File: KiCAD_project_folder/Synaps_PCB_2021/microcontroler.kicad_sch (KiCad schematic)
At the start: 35 parts, among them IC2 ESP32-S2, SW3 SW_Push, SW4 SW_Push, U3 AT25DF041x-UxN-x, Y2 40 MHz, Y3 32.768 KHz

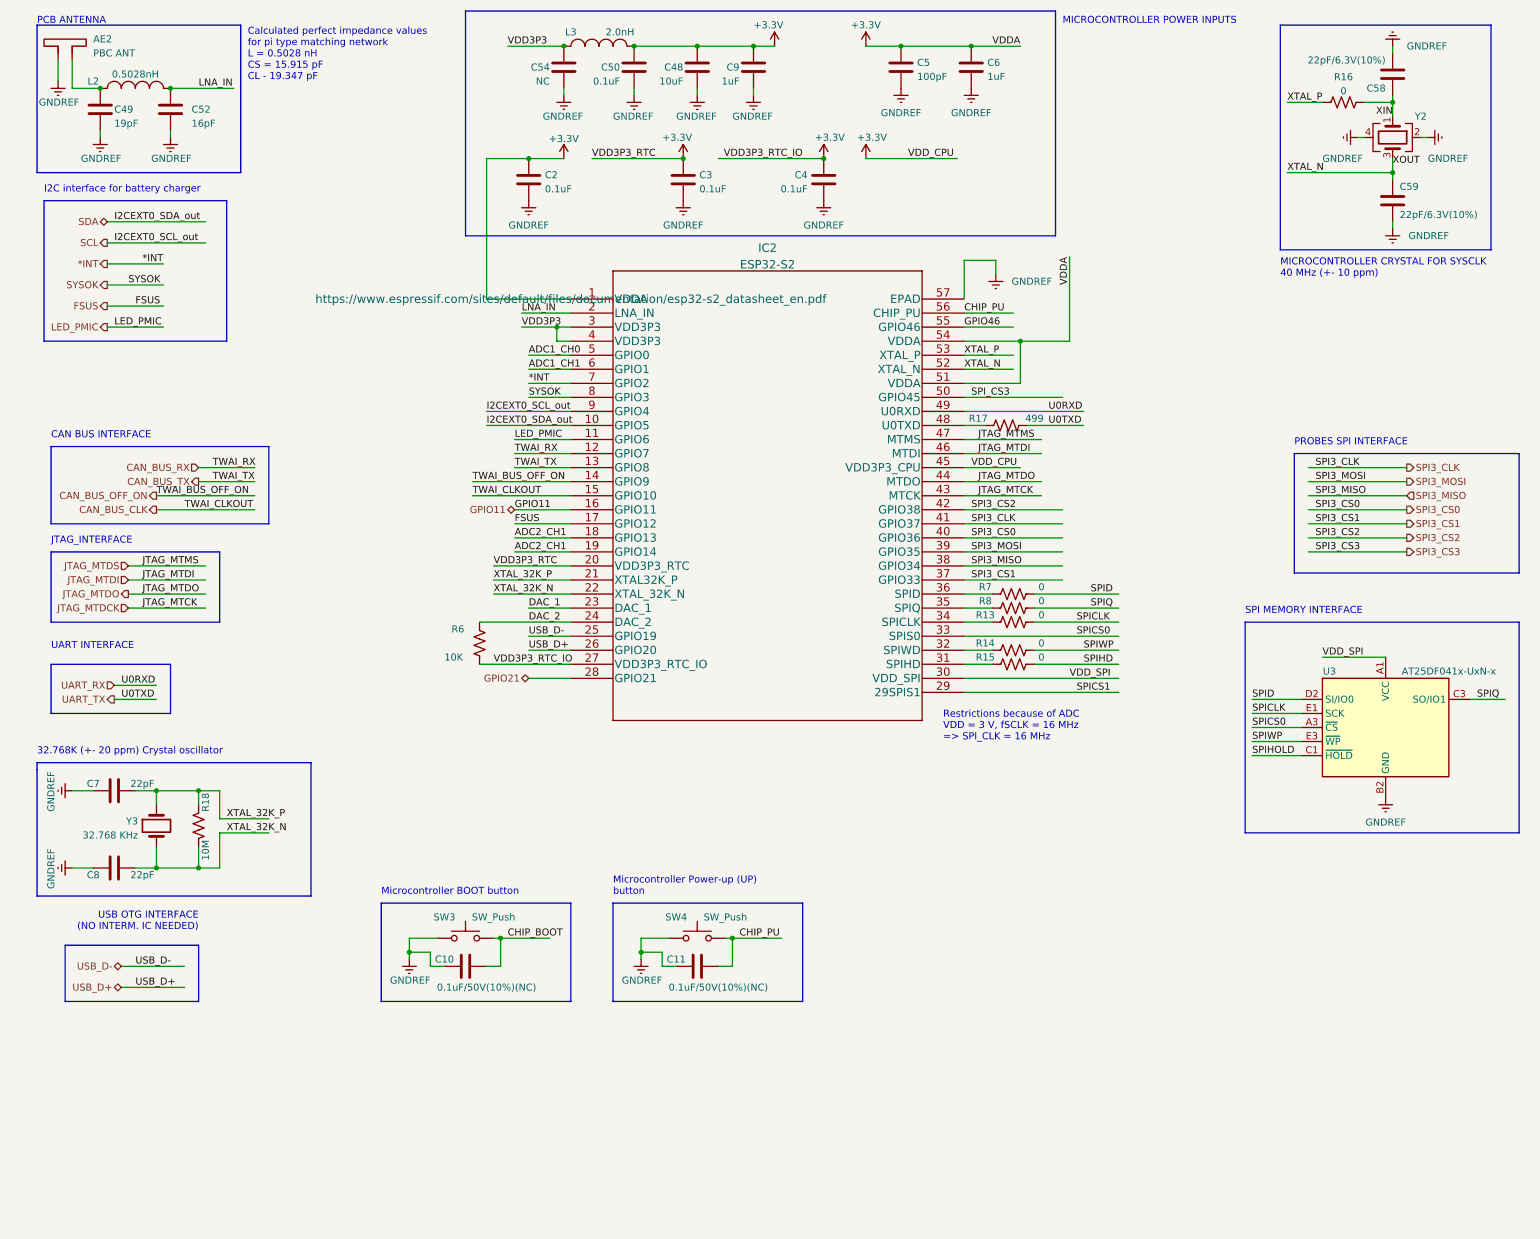
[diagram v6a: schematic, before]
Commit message: Transistionned board to ESP32S3, wip
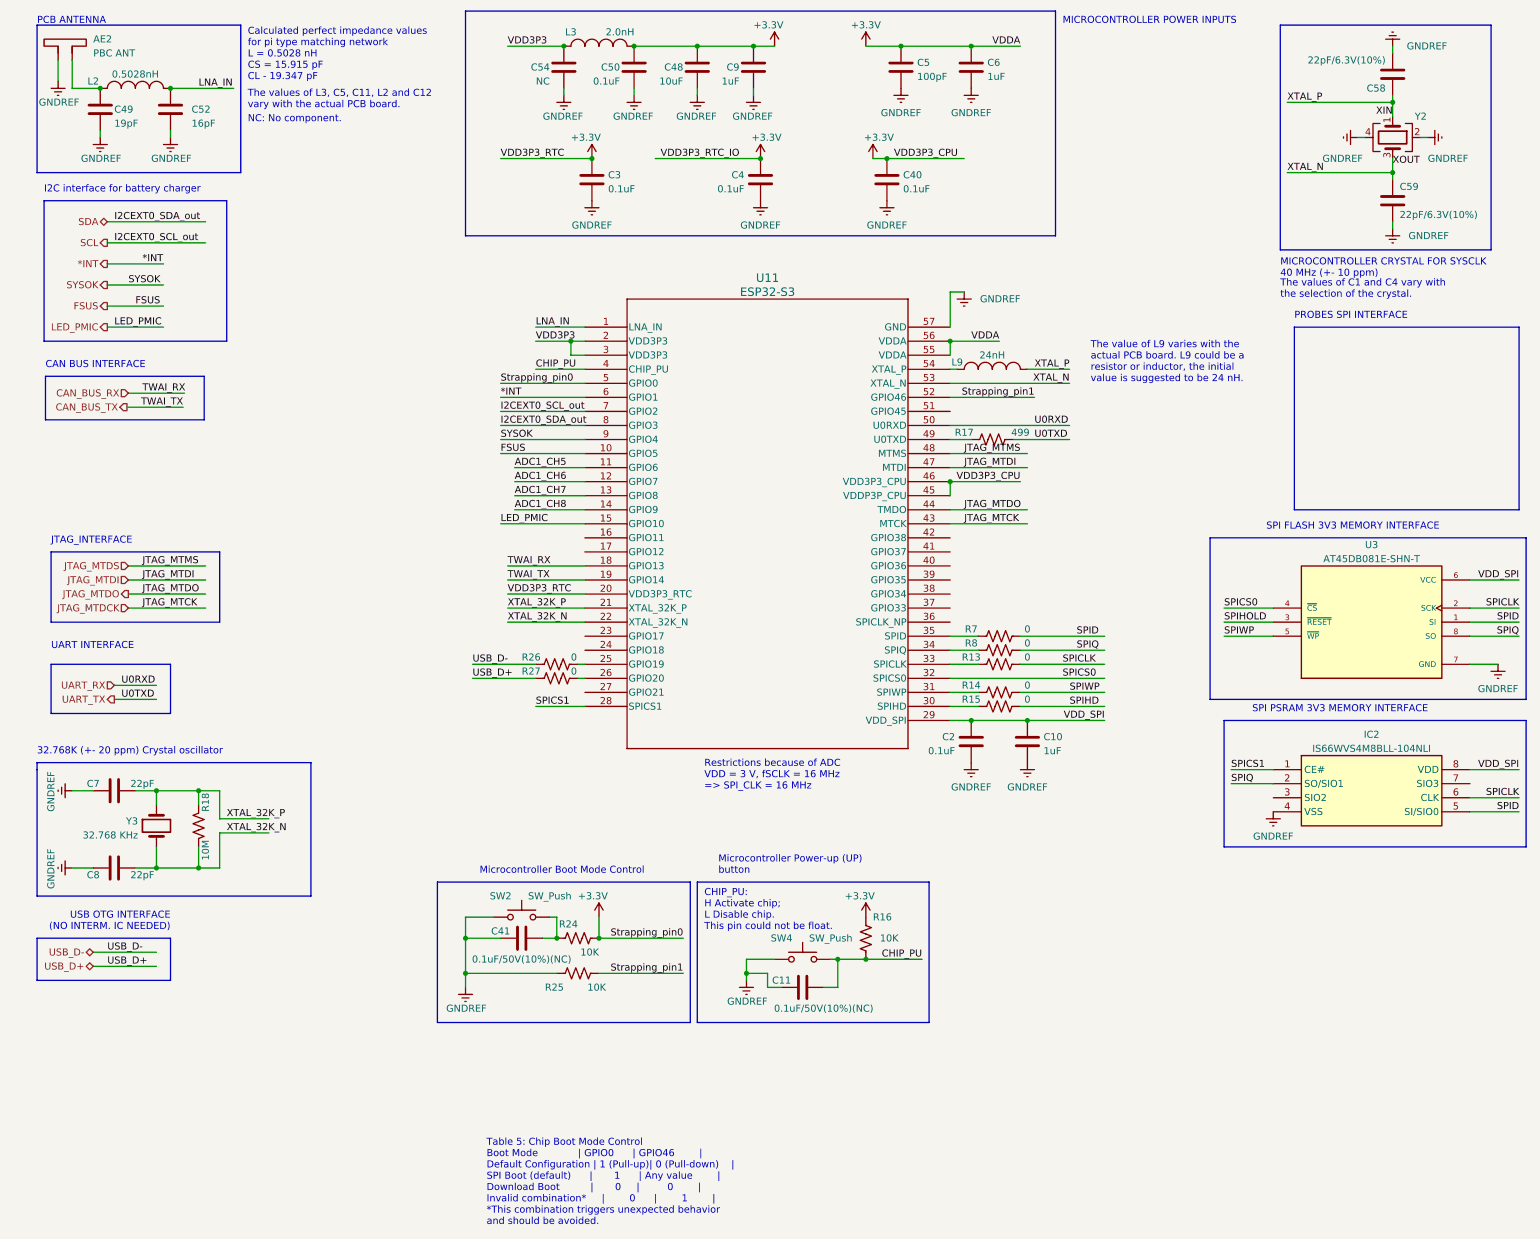
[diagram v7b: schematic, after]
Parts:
- removed IC2: ESP32-S2, ESP32-S2:ESP32-S2, symbol ESP32-S2:ESP32-S2
- removed R6: 10K, Resistor_SMD:R_1206_3216Metric_Pad1.30x1.75mm_HandSolder, symbol Device:R_US
- removed SW3: SW_Push, Push_Button:GPTS203211B, symbol Switch:SW_Push
- removed U3: AT25DF041x-UxN-x, Package_CSP:WLCSP-8_1.58x1.63x0.35mm_Layout3x5_P0.35x0.4mm_Ball0.25mm_Pad0.25mm_NSMD, symbol Memory_Flash:AT25DF041x-UxN-x
- added C40: 0.1uF, Capacitor_SMD:C_1206_3216Metric_Pad1.33x1.80mm_HandSolder, symbol Device:C
- added C41: 0.1uF/50V(10%)(NC), Capacitor_SMD:C_1206_3216Metric_Pad1.33x1.80mm_HandSolder, symbol Device:C
- added IC2: IS66WVS4M8BLL-104NLI, SOIC127P600X175-8N, symbol IS66WVS4M8BLL-104NLI:IS66WVS4M8BLL-104NLI
- added L9: 24nH, Inductor_SMD:L_1206_3216Metric_Pad1.22x1.90mm_HandSolder, symbol pspice:INDUCTOR
- added R24, R25: 10K, symbol Device:R_US
- added R26, R27: 0, symbol Device:R_US
- added SW2: SW_Push, Push_Button:GPTS203211B, symbol Switch:SW_Push
- added U11: ESP32-S3, QFN56_7X7_EXP, symbol ESP32-S3:ESP32-S3
- added U3: AT45DB081E-SHN-T, SOIC127P798X216-8N, symbol AT45DB081E-SHN-T:AT45DB081E-SHN-T
- C10: value 0.1uF/50V(10%)(NC) -> 1uF; MPN CC1206KRX7R9BB104 -> GCM31MR71H105KA55L; Supplier Link https://www.digikey.ca/en/products/detail/yageo/CC1206KRX7R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 -> https://www.digikey.ca/en/products/detail/murata-electronic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
- R16: value 0 -> 10K; footprint Resistor_SMD:R_1206_3216Metric_Pad1.30x1.75mm_HandSolder -> (none); MPN RC1206JR-070RL -> (none); Supplier Link https://www.digikey.ca/en/products/detail/yageo/RC1206JR-07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 -> (none)
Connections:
- net CHIP_BOOT is gone; now on net VDD_SPI: C10.1
- net XTAL_P is gone; now on net +3V3: R16.1
- net *INT: now also U11.6 (GPIO1)
- net +3V3: now also C40.1, R24.2, U11.20 (VDD3P3_RTC), U11.45 (VDDP3P_CPU), U11.46 (VDD3P3_CPU), U11.5 (GPIO0), U11.55 (VDDA), U11.56 (VDDA); no longer C2.1
- net CAN_BUS_RX: now also U11.18 (GPIO13)
- net CAN_BUS_TX: now also U11.19 (GPIO14)
- net CHIP_PU: now also R16.2, U11.4 (CHIP_PU)
- net FSUS: now also U11.10 (GPIO5)
- net GNDREF: now also C40.2, C41.2, IC2.4 (VSS), R25.1, SW2.1, U11.57 (GND), U3.7 (GND)
- net JTAG_MTDCK: now also U11.43 (MTCK)
- net JTAG_MTDI: now also U11.47 (MTDI)
- net JTAG_MTDO: now also U11.44 (TMDO)
- net JTAG_MTDS: now also U11.48 (MTMS)
- net LED_PMIC: now also U11.15 (GPIO10)
- net LNA_IN: now also U11.1 (LNA_IN)
- net SCL: now also U11.7 (GPIO2)
- net SDA: now also U11.8 (GPIO3)
- net SPICLK: now also IC2.6 (CLK), U3.2 (SCK)
- net SPICS0: now also U11.32 (SPICS0), U3.4 (~{CS})
- net SPICS1: now also IC2.1 (CE#), U11.28 (SPICS1)
- net SPID: now also IC2.5 (SI/SIO0), U3.1 (SI)
- net SPIHOLD: now also U3.3 (~{RESET})
- net SPIQ: now also IC2.2 (SO/SIO1), U3.8 (SO)
- net SPIWP: now also U3.5 (~{WP})
- net SYSOK: now also U11.9 (GPIO4)
- net UART_RX: now also U11.50 (U0RXD)
- net USB_D+: now also R27.2
- net USB_D-: now also R26.2
- net VDD3P3: now also U11.2 (VDD3P3), U11.3 (VDD3P3)
- net VDD_SPI: now also C2.1, IC2.8 (VDD), U11.29 (VDD_SPI), U3.6 (VCC)
- net XIN: now also L9.2; no longer R16.2
- net XOUT: now also U11.53 (XTAL_N)
- net XTAL_32K_N: now also U11.22 (XTAL_32K_N)
- net XTAL_32K_P: now also U11.21 (XTAL_32K_P)
- net at R15.1: now also U11.30 (SPIHD)
- net at R14.1: now also U11.31 (SPIWP)
- net at R13.1: now also U11.33 (SPICLK)
- net at R8.1: now also U11.34 (SPIQ)
- net at R7.1: now also U11.35 (SPID)
- net at R17.1: now also U11.49 (U0TXD)
- new net: C41.1, R24.1, SW2.2
- new net: L9.1, U11.54 (XTAL_P)
- new net: R26.1, U11.25 (GPIO19)
- new net: R27.1, U11.26 (GPIO20)
- new net ADC1_CH5: U11.11 (GPIO6)
- new net ADC1_CH6: U11.12 (GPIO7)
- new net ADC1_CH7: U11.13 (GPIO8)
- new net ADC1_CH8: U11.14 (GPIO9)
- new net Strapping_pin1: R25.2, U11.52 (GPIO46)
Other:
- note added: "CHIP_PU: H Activate chip; L Disable chip. This pin could not be float."
- note added: "Microcontroller Boot Mode Control"
- note added: "NC: No component."
- note added: "SPI FLASH 3V3 MEMORY INTERFACE"
- note added: "SPI PSRAM 3V3 MEMORY INTERFACE"
- note added: "Table 5: Chip Boot Mode Control Boot Mode | GPIO0 | GPIO46 | Default Configuration | 1 (Pull-up)| 0 (Pull-down) | SPI Boot (default) | 1 | Any value | Download Boot | 0 | 0 | Invalid combination* | 0 | 1 | *This combination triggers unexpected behavior and should be avoided."
- note added: "The value of L9 varies with the actual PCB board. L9 could be a resistor or inductor, the initial value is suggested to be 24 nH."
- note added: "The values of C1 and C4 vary with the selection of the crystal."
- note added: "The values of L3, C5, C11, L2 and C12 vary with the actual PCB board."
- note removed: "Microcontroller BOOT button"
- note removed: "SPI MEMORY INTERFACE"
- moved on the sheet: C11, C3, C4, R13, R14, R15, R17, R7, R8, SW4
